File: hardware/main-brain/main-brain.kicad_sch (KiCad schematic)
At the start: 27 parts, among them J1 19V, J2 CAN+5V, J3 19V OUT, J4 I2S OUT, Q1 SI2301 class, Q2 2N7000, U1 SN65HVD230

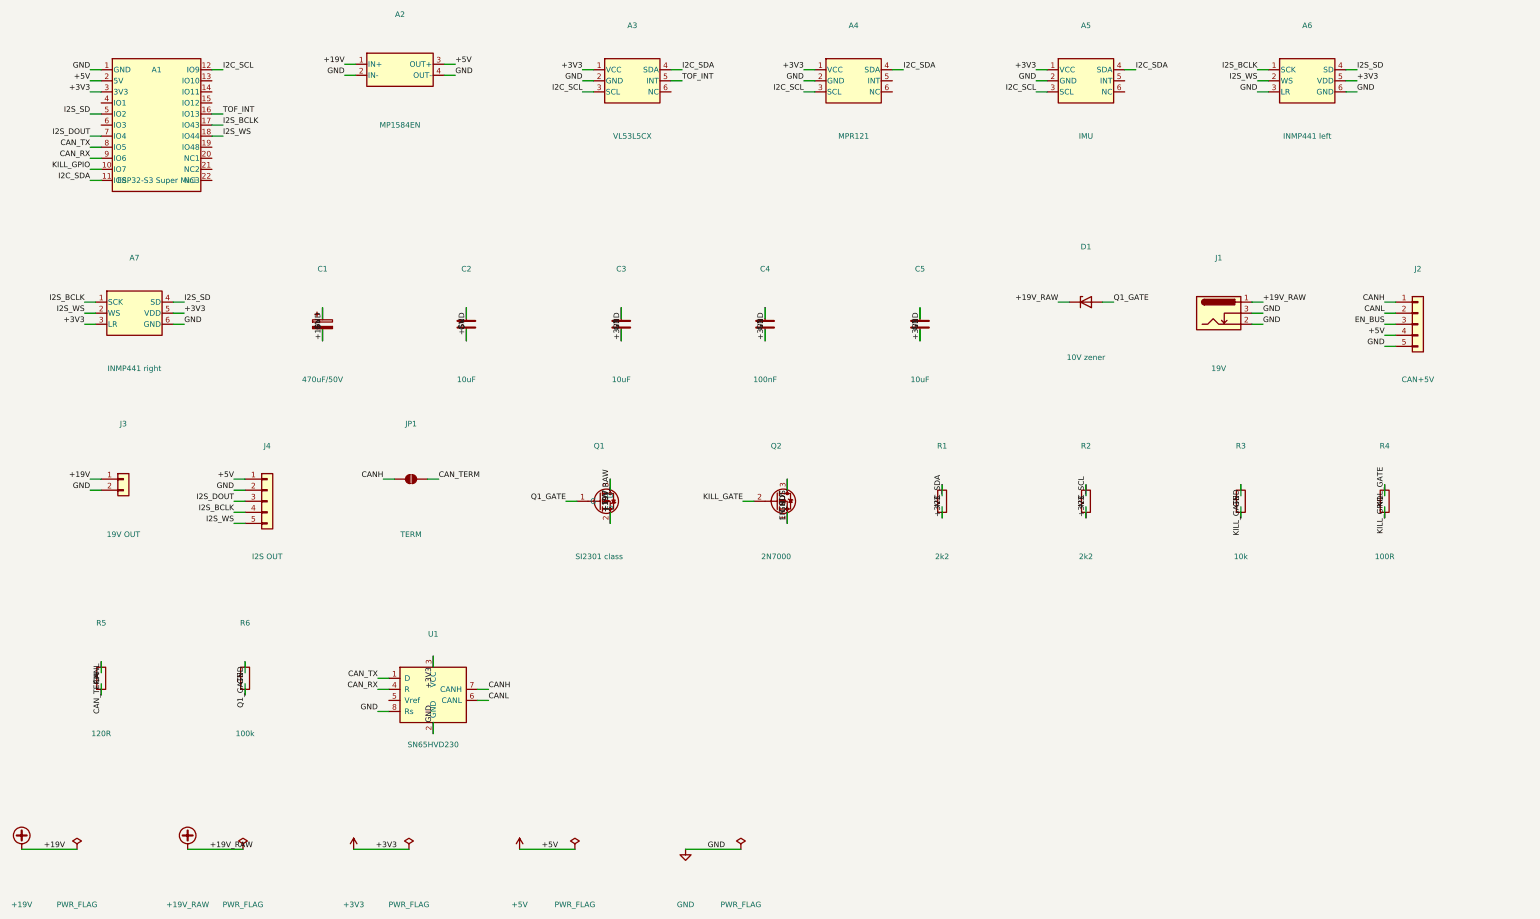
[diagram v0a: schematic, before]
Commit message: Rebuild both boards from the real driver module, grouped by function
The vendor's EasyEDA export of the driver module arrived, so its footprint is
now measured rather than guessed: 17 pins and four mounting holes over
22.6 x 18.2 mm, read from vendor/simplefoc_stepmini.json at build time.

The export also settles three things that were open, and raises one:

- The module's 3V3 pin is a supply input. Its nSLEEP and nRESET pull-ups hang
  off it and there is no regulator on the board, so leaving it open would have
  left the driver possibly held in reset. It is now wired to the 3.3 V rail.
- The header's enable pin sits behind a series resistor into the driver's EN,
  so the kill line drives it directly and nSLEEP/nRESET need no connection.
- nFAULT is brought out with its own pull-up, so it now goes to PB4.
- The export shows a quad half-bridge - IN1-IN4 and OUT1-OUT4 - not the
  three-in/three-out DRV8313 the build console names. A 3-phase motor uses
  three of the four channels, so it works, but it is not the specified part.
  Flagged in the actuator README rather than silently accepted.

Placement is now by functional block. Each block keeps its own passives, and
parts with an electrical reason to hug another are placed against it and
checked: the crystal is held within 12 mm of the MCU and its load caps within
9 mm of it, which the previous layout failed at 32 mm. Microphone spacing is
pinned at exactly 130 mm and verified. Both boards are larger - the node goes
to 70 x 60 and the base to 170 x 100 - which is what buys room to group and
still route by hand.

Indicators added on both boards, using the XL-3216SURC red 1206 that is on
hand. Series resistors are sized for its 2.4 V forward drop rather than left at
a default: 220 R on 3.3 V rails, 470 R on the 5 V one.

check.py grew to match: it now verifies group membership, pinned positions and
proximity constraints alongside the netlist, and each project carries a
colour-coded placement.svg.

Co-Authored-By: Claud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
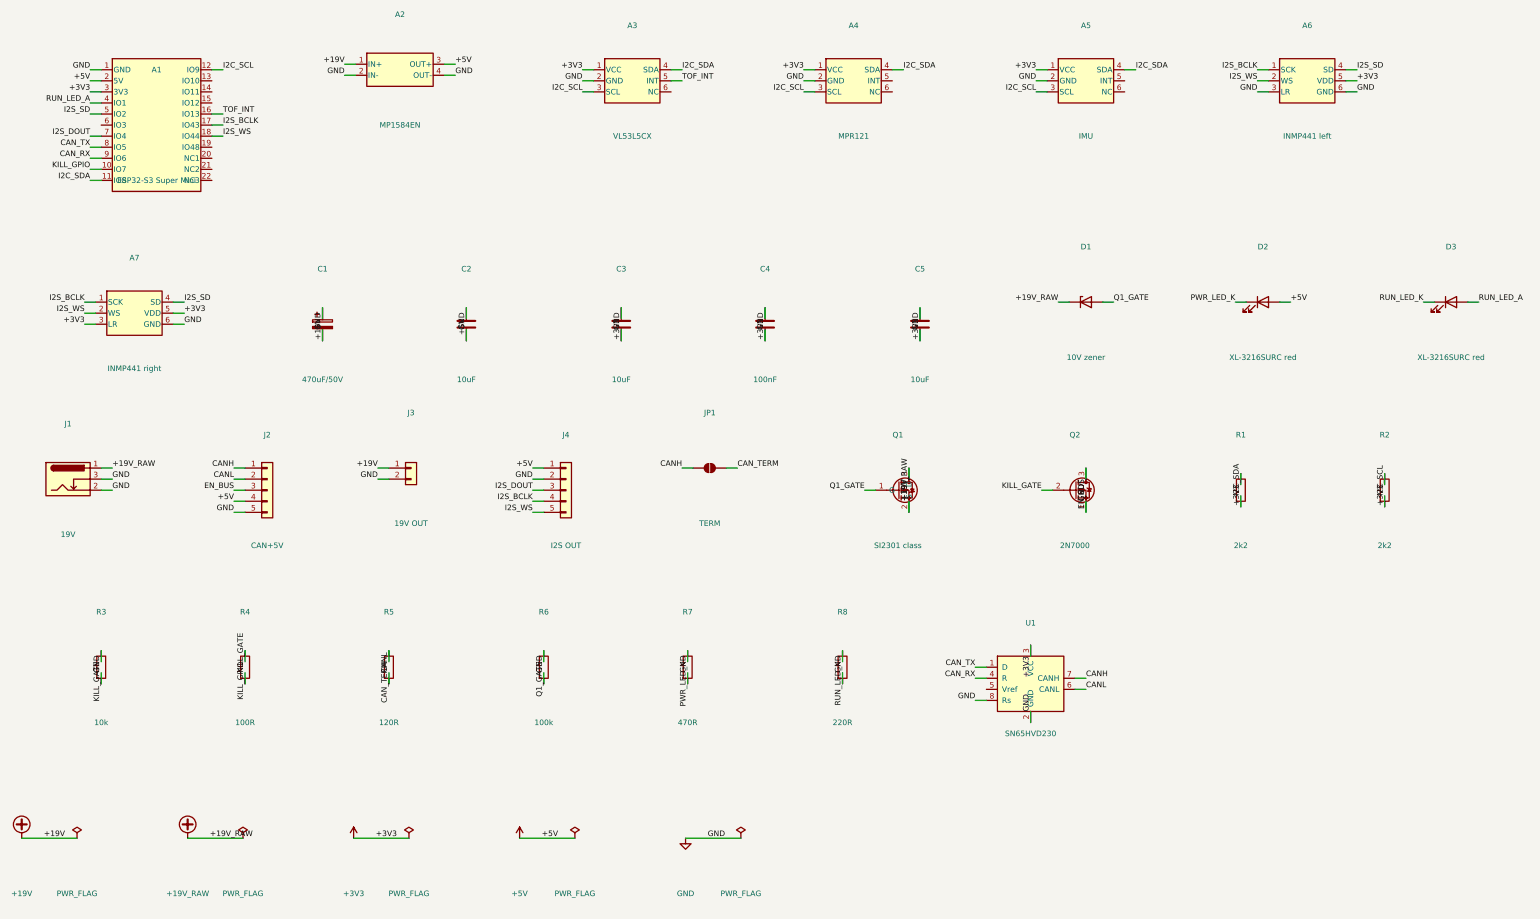
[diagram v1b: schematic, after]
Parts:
- added D2, D3: XL-3216SURC red, LED_SMD:LED_1206_3216Metric, symbol Device:LED
- added R7: 470R, Resistor_SMD:R_1206_3216Metric, symbol Device:R
- added R8: 220R, Resistor_SMD:R_1206_3216Metric, symbol Device:R
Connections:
- net +5V: now also D2.2 (A)
- net GND: now also R7.2, R8.2
- net RUN_LED_A: now reaches A1.4 (IO1)
- net RUN_LED_A: now also D3.2 (A)
- new net PWR_LED_K: D2.1 (K), R7.1
- new net RUN_LED_K: D3.1 (K), R8.1
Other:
- moved on the sheet: J1, J2, J3, J4, JP1, Q1, Q2, R1, R2, R3, R4, R5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

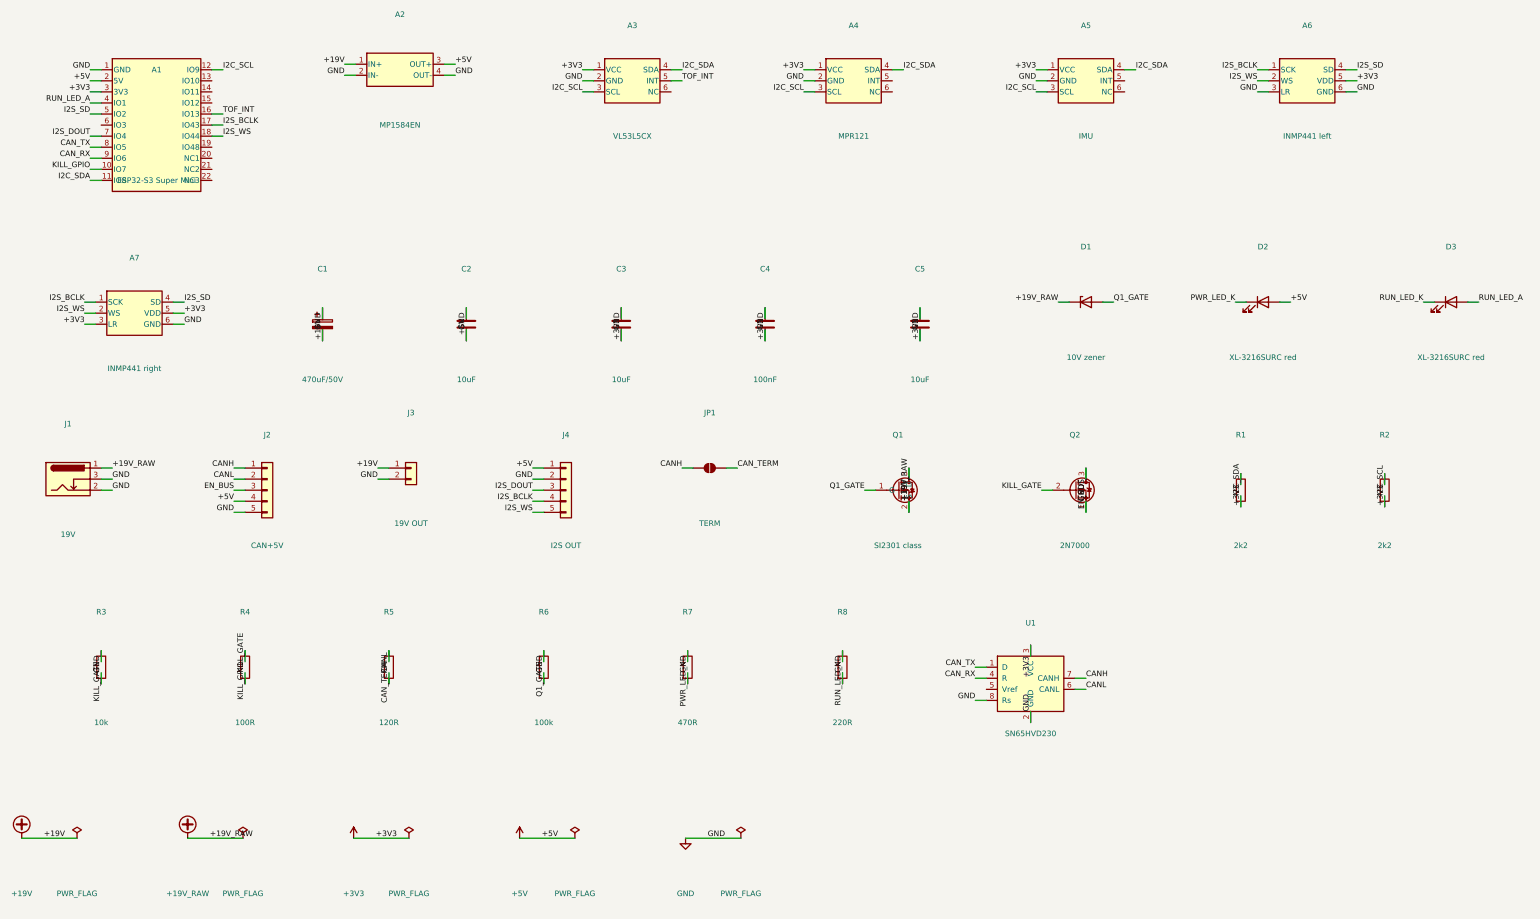
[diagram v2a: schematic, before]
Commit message: Rebuild the BOM around parts on hand, and target Lion Circuits
Every passive and semiconductor in both boards is now a part that is actually
on the shelf, with docs/parts.md recording the reconciliation. Four
substitutions were needed:

- LED series resistors move from 220R/470R, which are not stocked, to 120R on
  the 3.3 V rails (7.5 mA) and 1k on the brain's 5 V rail (2.6 mA, where 120R
  would exceed the LED's 20 mA rating).
- The kill-line gate series resistor moves from 100R to 120R, immaterial here.
- The reverse-polarity FET becomes the AO3481 that is actually on hand; KiCad
  has no symbol for it, so the projects use AO3401A, the same family and the
  same G/S/D pinout.
- The 10 V zener clamping that FET's gate is not stocked, so the gate is
  divided rather than clamped: 100k source-to-gate and 100k gate-to-ground put
  Vgs at about -9.5 V, which enhances the FET hard and stays well inside its
  rating. Two resistors that are stocked, replacing one part that is not.

Two items have no substitute and must be ordered: 30 mR shunts, without which
there is no current sensing, and an N-channel MOSFET for the kill line, since
the AO3481 on hand is P-channel and cannot pull the EN bus down. The kill line
is the one circuit that should not be improvised.

Also notes that the CD43 inductor supplied with the transceivers has no place
in either board, and why the one plausible use - an LC filter on the node's
5 V input - would resonate at about 28 kHz, right on top of the motor PWM.

For fabrication, the boards now carry plot settings that emit Protel-style
gerber extensions, matching the sample set from Lion Circuits, with the X2
attributes off so the output is plain RS-274X. docs/fabrication.md records
their file naming and the design rules used, and is explicit that their
capability page could not be reached from here, so those rules are a
conservative set rather than a reading of their spec sheet.

Co-Authored-By: Claude Opus 5 <noreply@anthropic.com>
Claude-Sess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
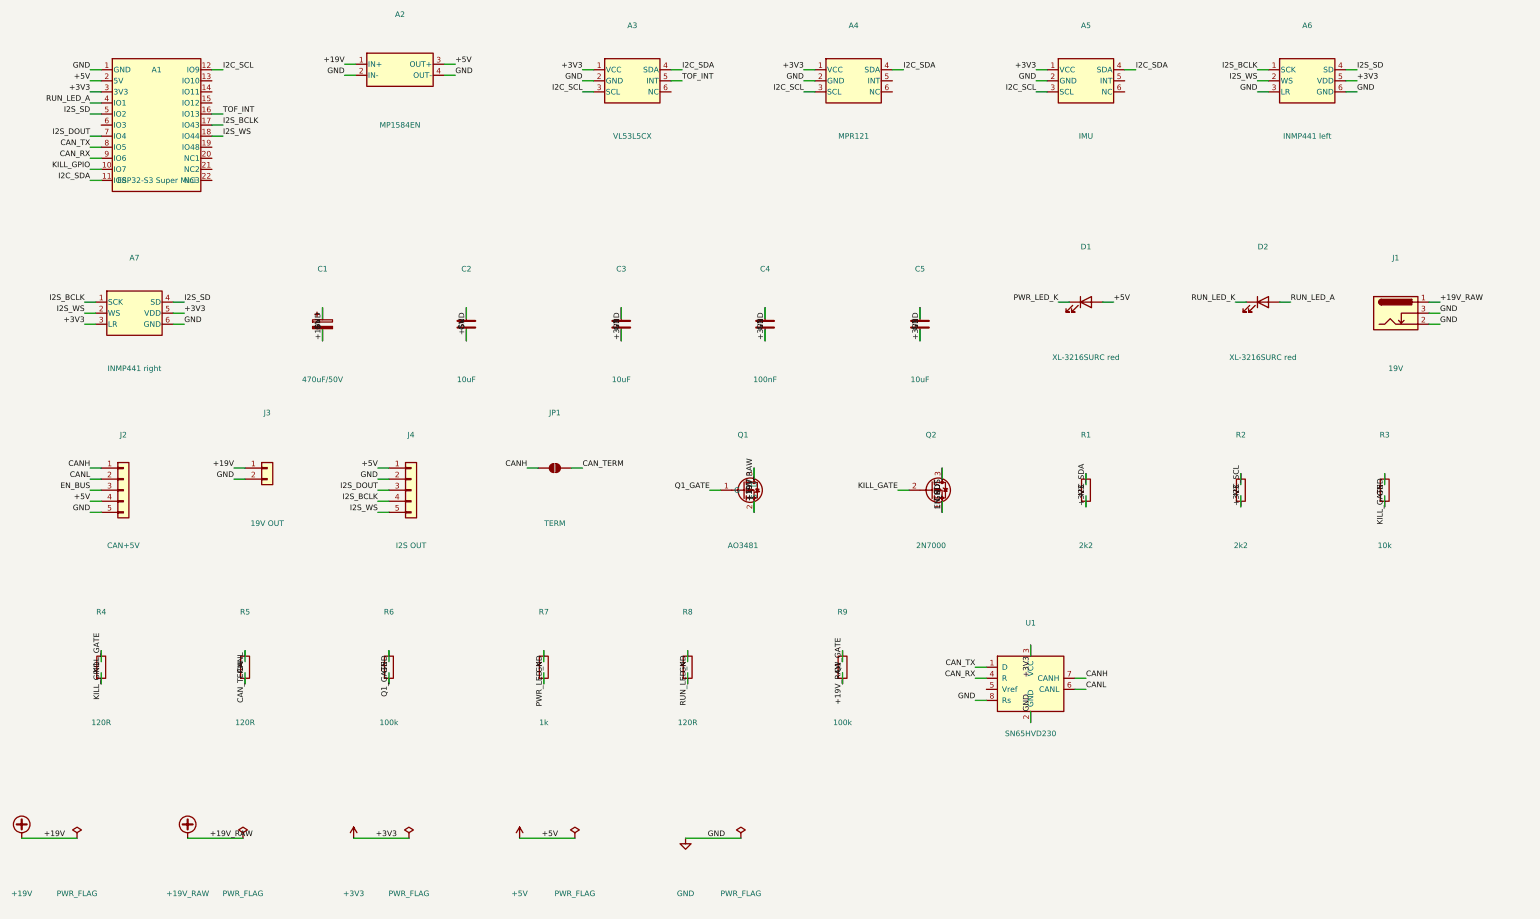
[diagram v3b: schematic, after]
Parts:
- removed D3: XL-3216SURC red, LED_SMD:LED_1206_3216Metric, symbol Device:LED
- added R9: 100k, Resistor_SMD:R_1206_3216Metric, symbol Device:R
- D1: value 10V zener -> XL-3216SURC red; footprint Diode_SMD:D_SOD-123 -> LED_SMD:LED_1206_3216Metric; symbol Device:D_Zener -> Device:LED
- Q1: value SI2301 class -> AO3481; symbol Transistor_FET:DMG2301L -> Transistor_FET:AO3401A
- R4: value 100R -> 120R
- R7: value 470R -> 1k
- R8: value 220R -> 120R
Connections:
- net +19V_RAW: now also R9.1; no longer D1.1 (K)
- net +5V: now also D1.2 (A); no longer D2.2 (A)
- net PWR_LED_K: now also D1.1 (K); no longer D2.1 (K)
- net Q1_GATE: now also R9.2; no longer D1.2 (A)
- net RUN_LED_A: now also D2.2 (A)
- net RUN_LED_K: now also D2.1 (K)
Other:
- moved on the sheet: J1, J2, J3, J4, JP1, Q1, Q2, R1, R2, R3, R4, R5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
